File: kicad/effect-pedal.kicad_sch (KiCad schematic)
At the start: 31 parts, among them J1 NJ3FD-V, J2 NJ3FD-V, J4 Conn_01x08, J5 Conn_01x09, J6 Conn_01x09, J7 Conn_ARM_JTAG_SWD_10, P2 USB_C_Plug_USB2.0, SW1 RotaryEncoder_Switch, SW2 RotaryEncoder_Switch, SW3 RotaryEncoder_Switch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

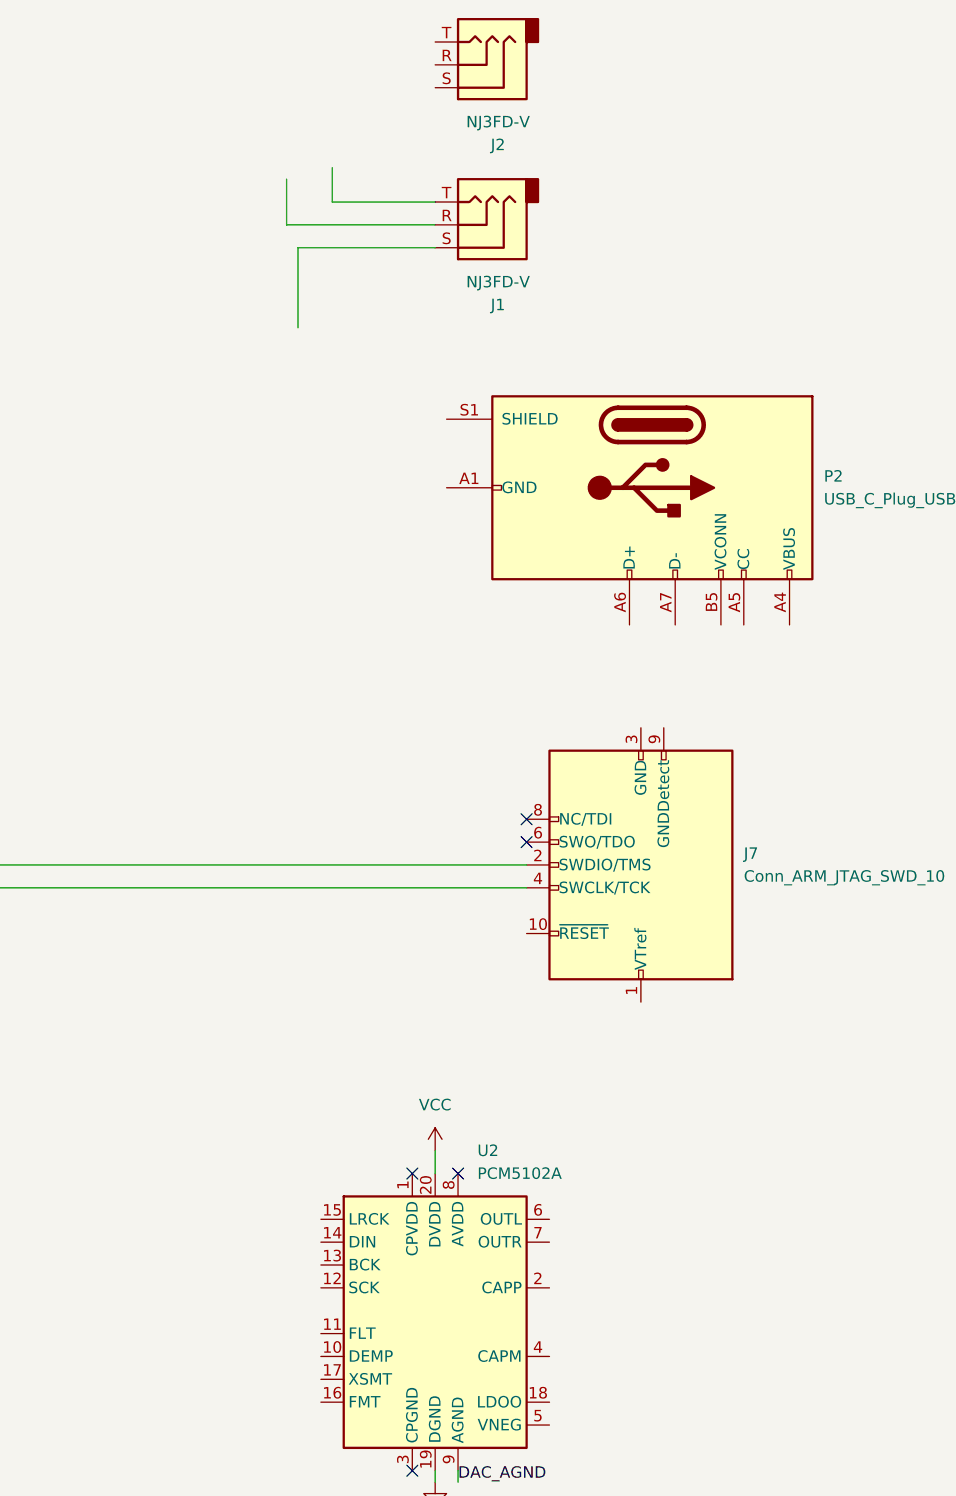
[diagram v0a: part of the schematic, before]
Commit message: wire up aud in jack
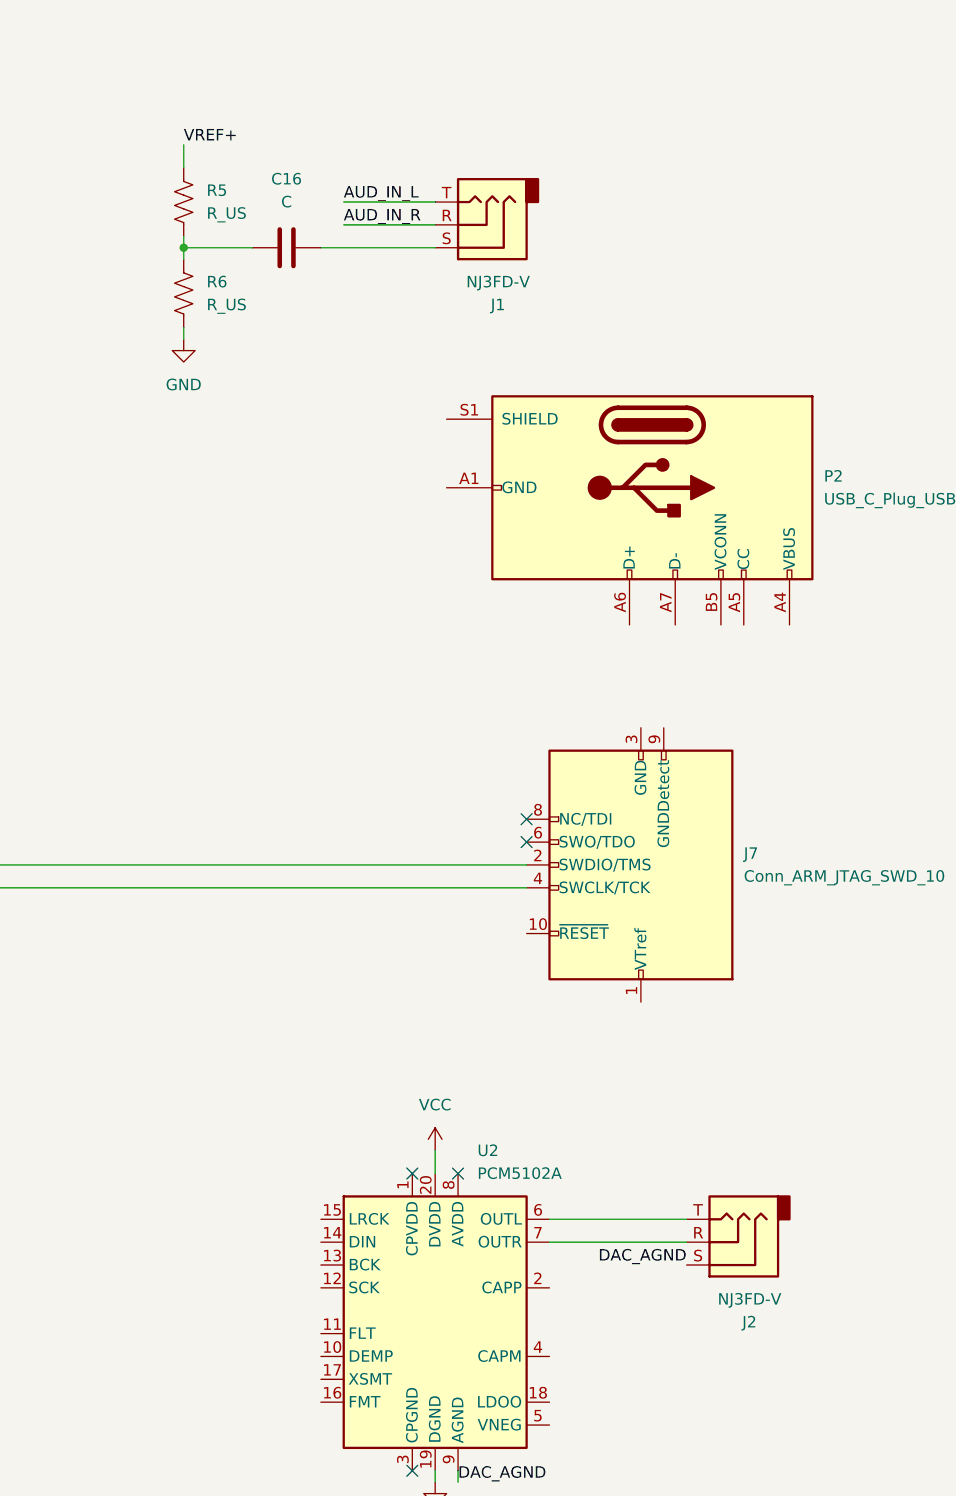
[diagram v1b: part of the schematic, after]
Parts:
- added C16: C, symbol Device:C
- added R5, R6: R_US, symbol Device:R_US
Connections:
- net AUD_IN_L: now also J1.T
- net AUD_IN_R: now also J1.R
- net DAC_AGND: now also J2.S
- net GND: now also R6.2
- net VREF+: now also R5.1
- net at J2.R: now also U2.7 (OUTR)
- net at J2.T: now also U2.6 (OUTL)
- net at J1.S: now also C16.2
- new net: C16.1, R5.2, R6.1
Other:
- moved on the sheet: J2

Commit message: start to DAC wiring
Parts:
- added C15: C, symbol Device:C
- added C17, C18, C22: .1u, symbol Device:C
- added C19, C20, C23: 10u, symbol Device:C_Polarized_US
- added C21: 2.2u, symbol Device:C
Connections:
- net EDAC_DOUT is gone; now on net EDAC_DATA: U1.123 (PD7)
- net EDAC_BCLK: now also U2.13 (BCK)
- net EDAC_FLT: now also U2.11 (FLT)
- net EDAC_FMT: now also U2.16 (FMT)
- net EDAC_LRCLK: now also U2.15 (LRCK)
- net EDAC_XSMT: now also U2.17 (XSMT)
- net GND: now also U2.12 (SCK), C17.2, C18.1, C19.2, C20.2; no longer U1.132 (PG15)
- net VCC: now also C18.2, C20.1, C22.1, C23.1
- net EDAC_DEMP: now reaches U2.10 (DEMP)
- net EDAC_DEMP: now also U1.132 (PG15)
- net EDAC_DATA: now reaches U2.14 (DIN)
- net at U2.18 (LDOO): now also C17.1, C19.1
- net at U2.2 (CAPP): now also C15.2
- net AGND: now reaches U2.3 (CPGND)
- net AGND: now also C21.1, C22.2, C23.2
- net at U2.4 (CAPM): now also C15.1
- net at U2.5 (VNEG): now also C21.2
- no-connect marks 7 -> 6
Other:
- moved on the sheet: C16, J1, R5, R6
